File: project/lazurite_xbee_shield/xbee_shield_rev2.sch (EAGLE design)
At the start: 2 parts

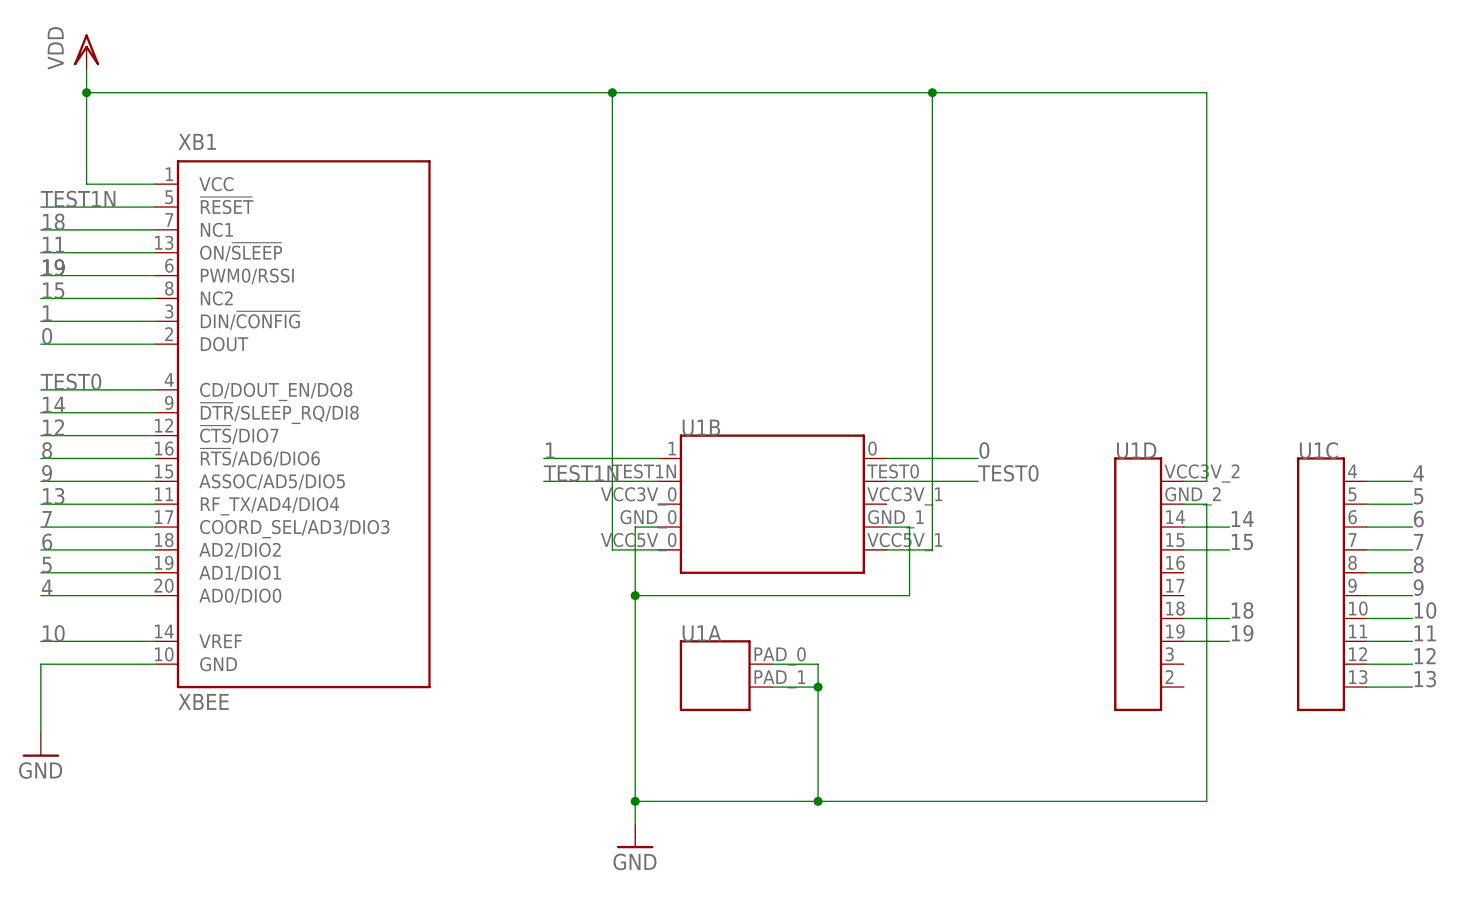
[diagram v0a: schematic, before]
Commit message: update libraries and all schematic/board data.
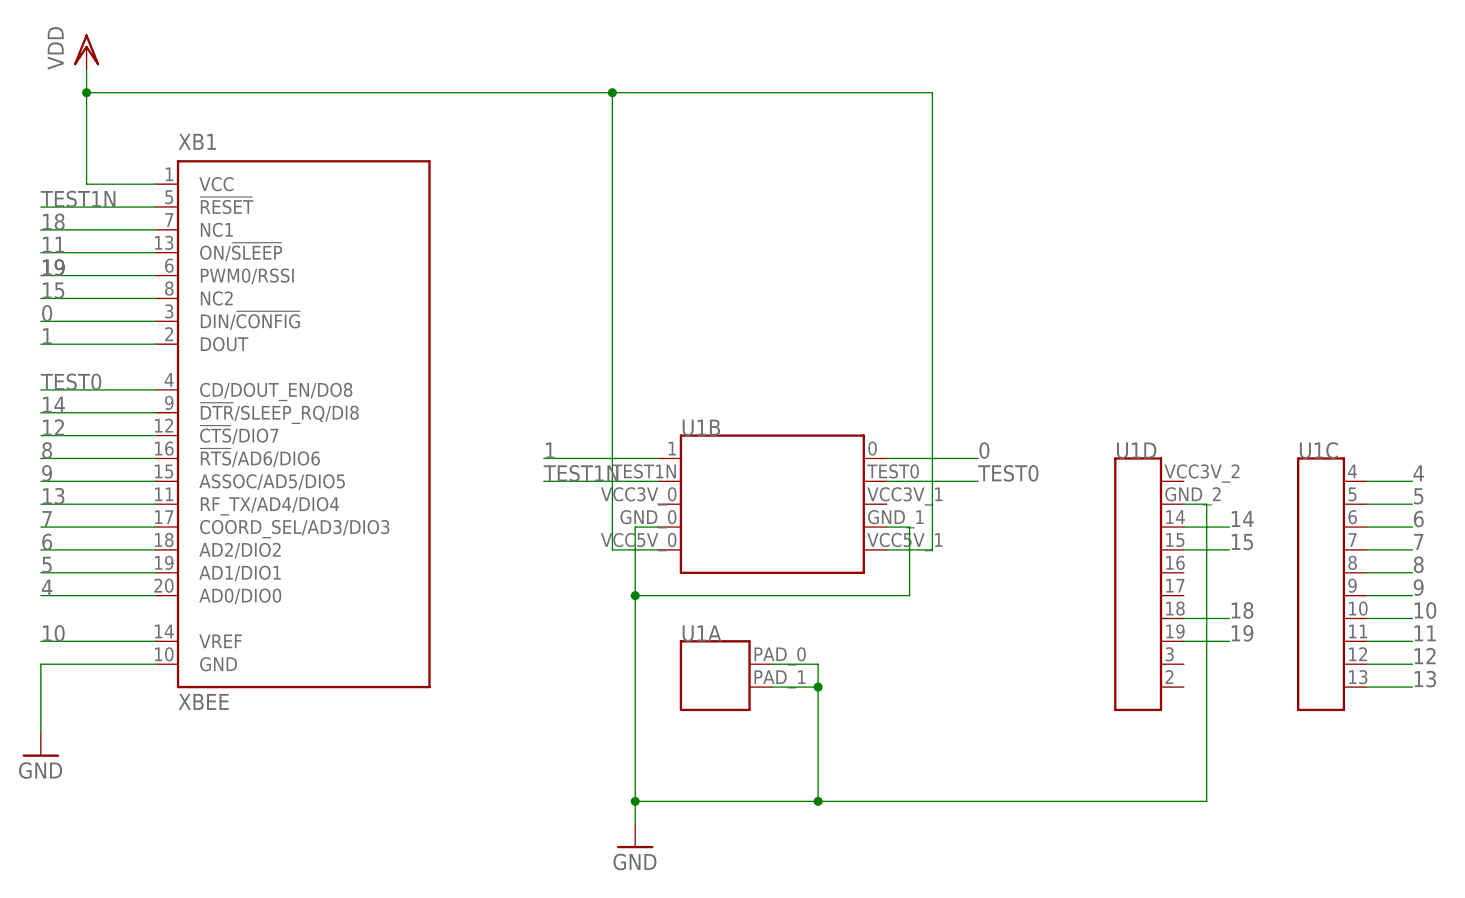
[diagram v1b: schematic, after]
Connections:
- net 0: now also XB1.DIN/!CONFIG; no longer XB1.DOUT
- net 1: now also XB1.DOUT; no longer XB1.DIN/!CONFIG
- net VDD: no longer U1D.VCC3V_2
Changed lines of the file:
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@@
 <net name="0" class="0">
-<segment>
-<pinref part="XB1" gate="G$1" pin="DOUT"/>
-<wire x1="7.62" y1="68.58" x2="-5.08" y2="68.58" width="0.1524" layer="91"/>
-<label x="-5.08" y="68.58" size="1.778" layer="95"/>
-</segment>
 <segment>
 <pinref part="U1" gate="B" pin="0"/>
@@
 <label x="99.06" y="55.88" size="1.778" layer="95"/>
 </segment>
-</net>
-<net name="1" class="0">
 <segment>
 <pinref part="XB1" gate="G$1" pin="DIN/!CONFIG"/>
@@
 <label x="-5.08" y="71.12" size="1.778" layer="95"/>
 </segment>
+</net>
+<net name="1" class="0">
 <segment>
 <pinref part="U1" gate="B" pin="1"/>
 <wire x1="63.5" y1="55.88" x2="50.8" y2="55.88" width="0.1524" layer="91"/>
 <label x="50.8" y="55.88" size="1.778" layer="95"/>
+</segment>
+<segment>
+<pinref part="XB1" gate="G$1" pin="DOUT"/>
+<wire x1="7.62" y1="68.58" x2="-5.08" y2="68.58" width="0.1524" layer="91"/>
+<label x="-5.08" y="68.58" size="1.778" layer="95"/>
 </segment>
 </net>
@@
 <wire x1="93.98" y1="96.52" x2="93.98" y2="45.72" width="0.1524" layer="91"/>
 <junction x="58.42" y="96.52"/>
-<wire x1="93.98" y1="96.52" x2="124.46" y2="96.52" width="0.1524" layer="91"/>
-<wire x1="124.46" y1="96.52" x2="124.46" y2="53.34" width="0.1524" layer="91"/>
-<junction x="93.98" y="96.52"/>
-<pinref part="U1" gate="D" pin="VCC3V_2"/>
-<wire x1="124.46" y1="53.34" x2="121.92" y2="53.34" width="0.1524" layer="91"/>
 <pinref part="VDD1" gate="G$1" pin="VDD"/>
 <wire x1="0" y1="99.06" x2="0" y2="96.52" width="0.1524" layer="91"/>
